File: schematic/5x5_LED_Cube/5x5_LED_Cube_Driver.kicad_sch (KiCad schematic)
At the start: 18 parts, among them J1 Conn_01x07, J2 Power, J3 Layers, Q1 DMG2305UX, Q2 DMG2305UX, Q3 DMG2305UX, Q4 DMG2305UX, Q5 DMG2305UX, U1 TLC5940NT, U2 TLC5940NT

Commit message: Added pico symbol to schematic
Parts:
- added U3: Pico, RPi_Pico:RPi_Pico_SMD_TH, symbol MCU_RaspberryPi_and_Boards:Pico
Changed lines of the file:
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@@
+    )
+  )
+  (symbol (lib_id "MCU_RaspberryPi_and_Boards:Pico") (at 78.74 148.59 0) (unit 1)
+    (in_bom yes) (on_board yes) (dnp no) (fields_autoplaced)
+    (property "Reference" "U3" (at 78.74 119.0371 0)
+      (effects (font (size 1.27 1.27)))
+    )
+    (property "Value" "Pico" (at 78.74 120.9581 0)
+      (effects (font (size 1.27 1.27)))
+    )
+    (property "Footprint" "RPi_Pico:RPi_Pico_SMD_TH" (at 78.74 148.59 90)
+      (effects (font (size 1.27 1.27)) hide)
+    )
+    (property "Datasheet" "" (at 78.74 148.59 0)
+      (effects (font (size 1.27 1.27)) hide)
+    )
+    (pin "1")
+    (pin "10")
+    (pin "11")
+    (pin "12")
+    (pin "13")
+    (pin "14")
+    (pin "15")
+    (pin "16")
+    (pin "17")
+    (pin "18")
+    (pin "19")
+    (pin "2")
+    (pin "20")
+    (pin "21")
+    (pin "22")
+    (pin "23")
+    (pin "24")
+    (pin "25")
+    (pin "26")
+    (pin "27")
+    (pin "28")
+    (pin "29")
+    (pin "3")
+    (pin "30")
+    (pin "31")
+    (pin "32")
+    (pin "33")
+    (pin "34")
+    (pin "35")
+    (pin "36")
+    (pin "37")
+    (pin "38")
+    (pin "39")
+    (pin "4")
+    (pin "40")
+    (pin "41")
+    (pin "42")
+    (pin "43")
+    (pin "5")
+    (pin "6")
+    (pin "7")
+    (pin "8")
+    (pin "9")
+    (instances
+      (project "5x5_LED_Cube_Driver"
+        (path "/3c8dc442-e2f5-4a62-b376-6357b309533c"
+          (reference "U3") (unit 1)
+        )
+      )
     )
   )

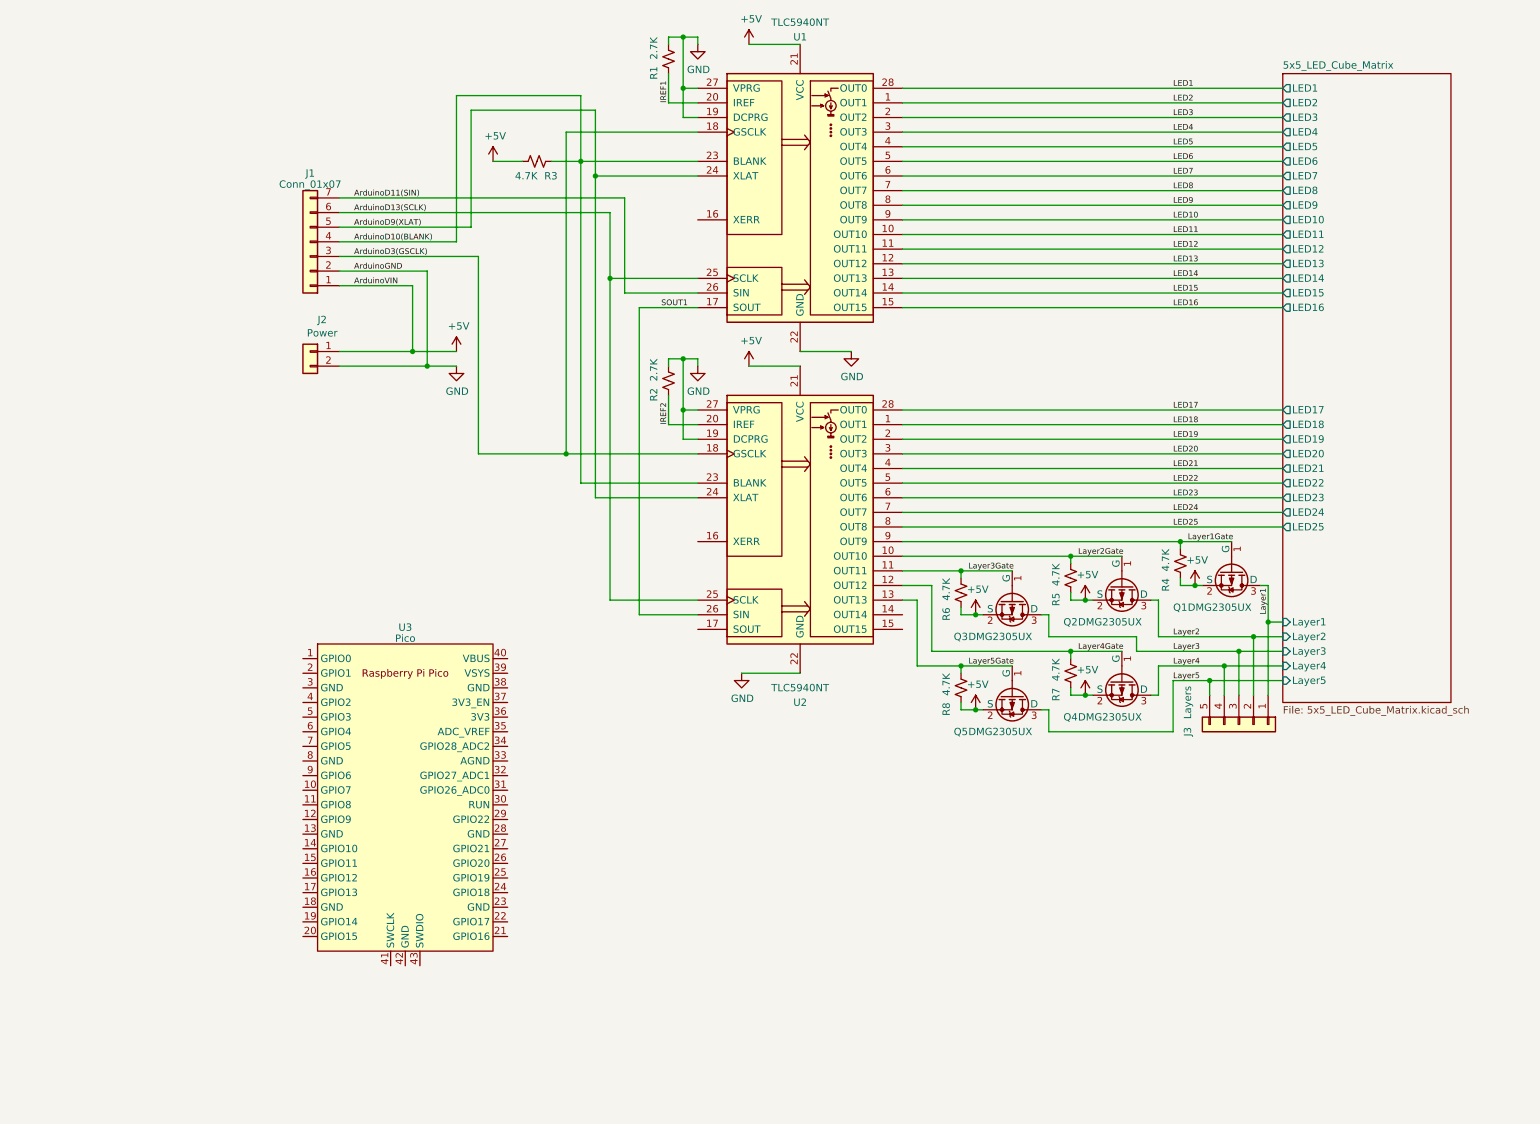
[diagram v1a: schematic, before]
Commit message: Updated schematic to include the RPi Pico and SD card module
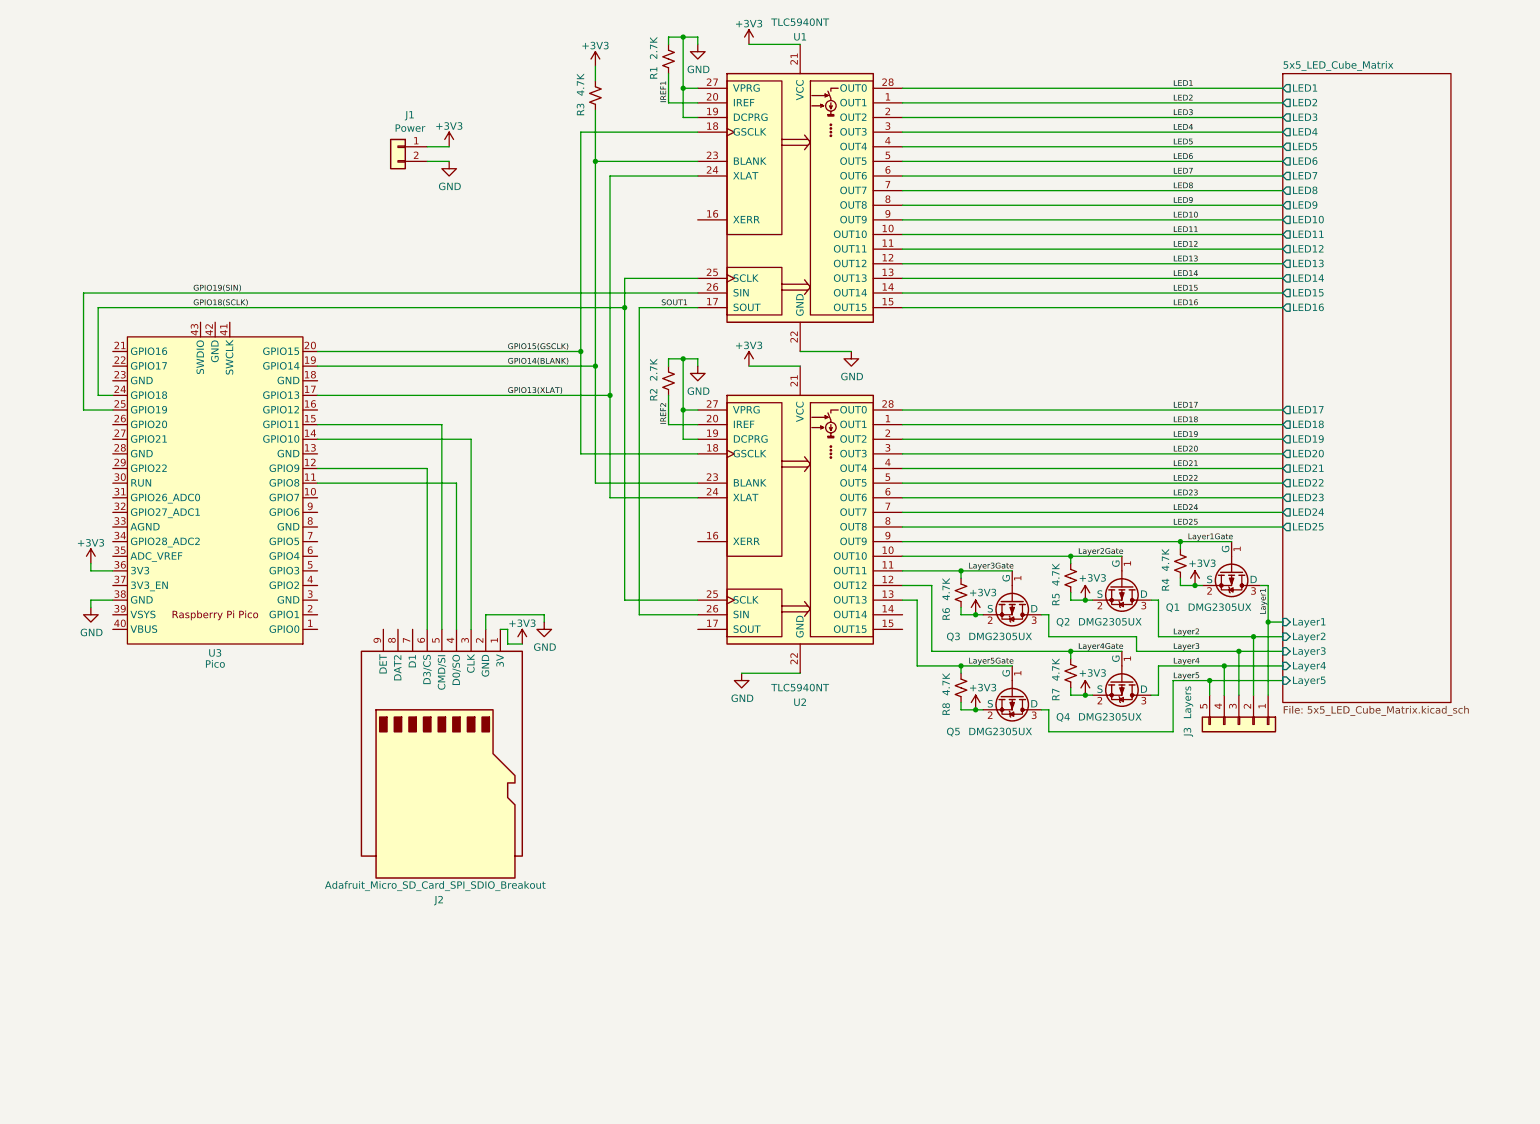
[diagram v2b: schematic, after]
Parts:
- removed J1: Conn_01x07, symbol Connector_Generic:Conn_01x07
- added J2: Adafruit_Micro_SD_Card_SPI_SDIO_Breakout, Connector_PinHeader_2.00mm:PinHeader_1x09_P2.00mm_Vertical, symbol My_Library:Adafruit_Micro_SD_Card_SPI_SDIO_Breakout
- renumbered J2 to J1
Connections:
- net +5V is gone; now on net +3V3: J1.1 (Pin_1), Q1.2 (S), Q2.2 (S), Q3.2 (S), Q4.2 (S), Q5.2 (S), R3.2, R4.1, R5.1, R6.1, R7.1, R8.1, U1.21 (VCC), U2.21 (VCC)
- net ArduinoD10(BLANK) is gone; now on net GPIO14(BLANK): R3.1, U1.23 (BLANK), U2.23 (BLANK)
- net ArduinoD11(SIN) is gone; now on net GPIO19(SIN): U1.26 (SIN)
- net ArduinoD13(SCLK) is gone; now on net GPIO18(SCLK): U1.25 (SCLK), U2.25 (SCLK)
- net ArduinoD3(GSCLK) is gone; now on net GPIO15(GSCLK): U1.18 (GSCLK), U2.18 (GSCLK)
- net ArduinoD9(XLAT) is gone; now on net GPIO13(XLAT): U1.24 (XLAT), U2.24 (XLAT)
- net GND: now also U3.38 (GND), J2.2 (GND)
- net at U3.11 (GPIO8): now also J2.4 (D0/SO)
- net at U3.12 (GPIO9): now also J2.6 (D3/CS)
- net at U3.14 (GPIO10): now also J2.3 (CLK)
- net at U3.15 (GPIO11): now also J2.5 (CMD/SI)
- net GPIO13(XLAT): now reaches U3.17 (GPIO13)
- net GPIO14(BLANK): now reaches U3.19 (GPIO14)
- net GPIO15(GSCLK): now reaches U3.20 (GPIO15)
- net GPIO18(SCLK): now reaches U3.24 (GPIO18)
- net GPIO19(SIN): now reaches U3.25 (GPIO19)
- net +3V3: now reaches U3.36 (3V3)
- net +3V3: now also J2.1 (3V)
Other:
- moved on the sheet: J1, R3, U3

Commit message: Updated schematic to wire up the SD card module to the pico
Signed-off-by: crash8229 <mu304007@gmail.com>
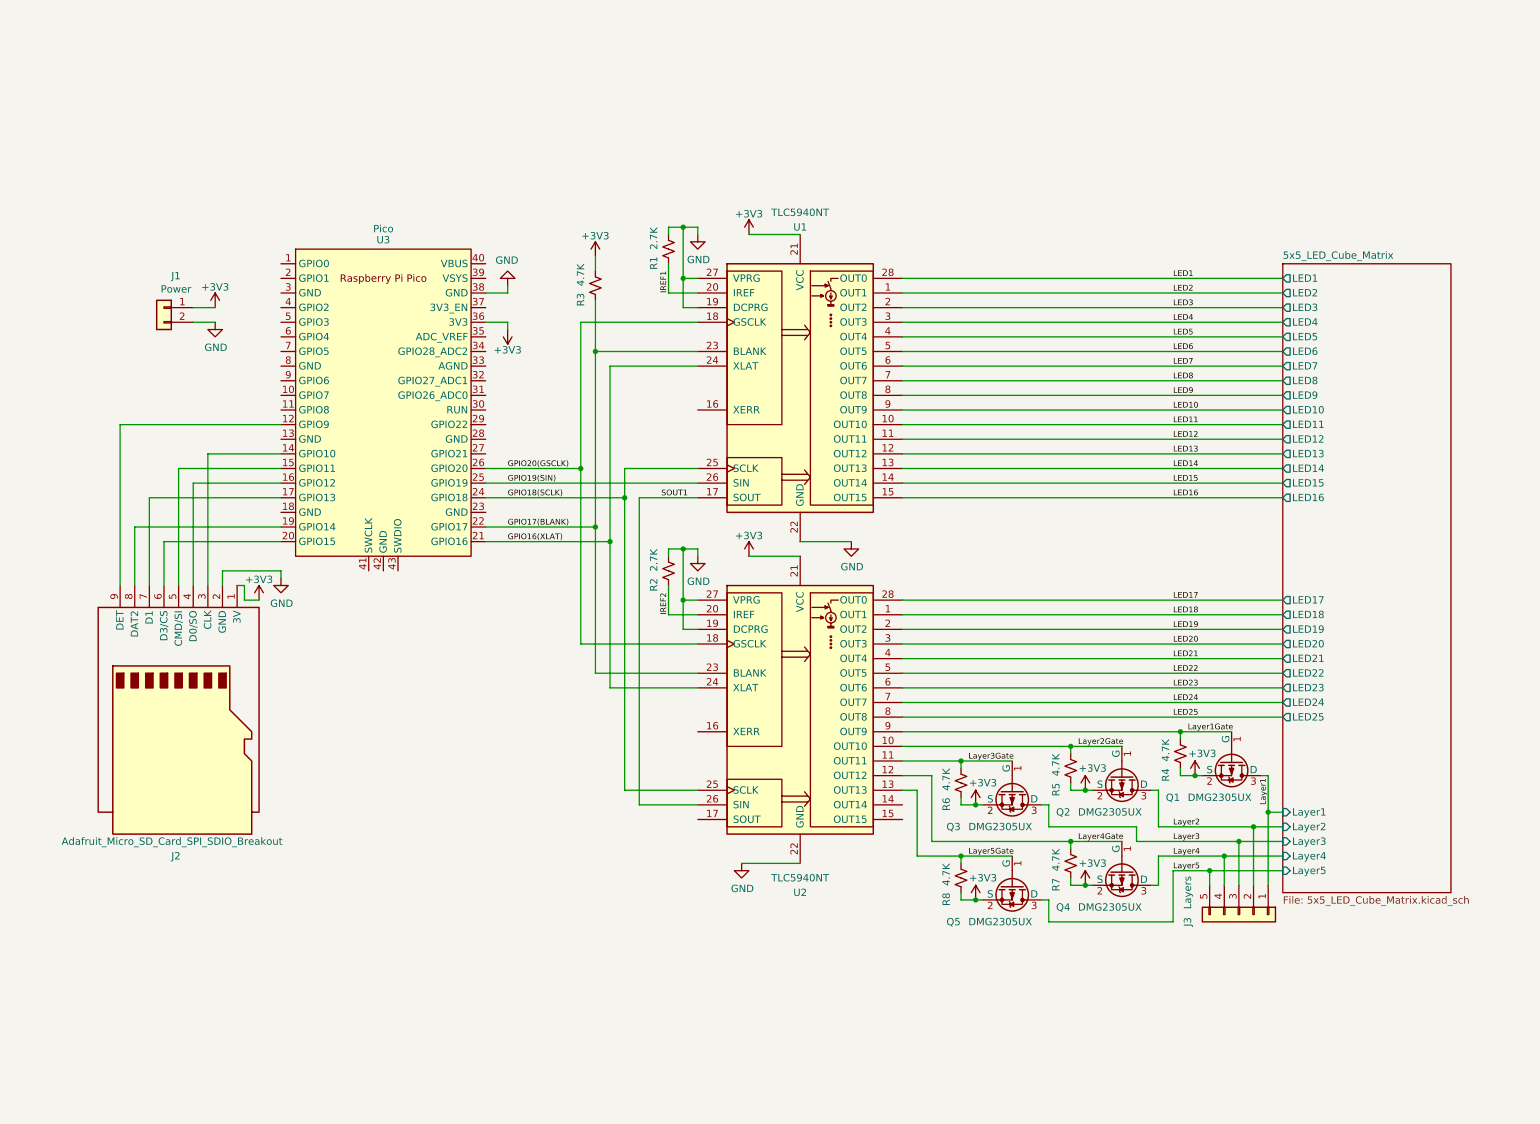
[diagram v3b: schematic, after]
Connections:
- net at J2.4 (D0/SO): now also U3.16 (GPIO12); no longer U3.11 (GPIO8)
- net at J2.6 (D3/CS): now also U3.20 (GPIO15); no longer U3.12 (GPIO9)
- net at J2.7 (D1): now also U3.17 (GPIO13)
- net at J2.8 (DAT2): now also U3.19 (GPIO14)
- net at J2.9 (DET): now also U3.12 (GPIO9)
- net GPIO16(XLAT): now reaches U3.21 (GPIO16)
- net GPIO16(XLAT): now also U1.24 (XLAT), U2.24 (XLAT)
- net GPIO17(BLANK): now reaches U3.22 (GPIO17)
- net GPIO17(BLANK): now also R3.1, U1.23 (BLANK), U2.23 (BLANK)
- net GPIO20(GSCLK): now reaches U3.26 (GPIO20)
- net GPIO20(GSCLK): now also U1.18 (GSCLK), U2.18 (GSCLK)
- removed net GPIO13(XLAT): U1.24 (XLAT), U2.24 (XLAT), U3.17 (GPIO13)
- removed net GPIO14(BLANK): R3.1, U1.23 (BLANK), U2.23 (BLANK), U3.19 (GPIO14)
- removed net GPIO15(GSCLK): U1.18 (GSCLK), U2.18 (GSCLK), U3.20 (GPIO15)
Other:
- moved on the sheet: J1, J2, J3, Q1, Q2, Q3, Q4, Q5, R1, R2, R3, R4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

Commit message: Updated schematic and footprints
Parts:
- added C1, C2, C3, C4: 0.1µF, Capacitor_SMD:C_0402_1005Metric_Pad0.74x0.62mm_HandSolder, symbol Device:C_Small
- J1: footprint Connector_PinHeader_2.00mm:PinHeader_1x02_P2.00mm_Vertical -> Connector_PinSocket_2.54mm:PinSocket_1x02_P2.54mm_Vertical
- J2: footprint Connector_PinHeader_2.00mm:PinHeader_1x09_P2.00mm_Vertical -> My_Library:Adafruit_Micro_SD_Card_SPI_SDIO_Breakout
- J3: footprint Connector_PinHeader_2.00mm:PinHeader_1x05_P2.00mm_Vertical -> Connector_PinSocket_2.54mm:PinSocket_1x05_P2.54mm_Vertical
- U3: footprint RPi_Pico:RPi_Pico_SMD_TH -> MCU_RaspberryPi_and_Boards:RPi_Pico_SMD_TH
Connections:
- net +3V3: now also U3.39 (VSYS), C1.1, C2.2, C3.1, C4.2; no longer U3.36 (3V3)
- net GND: now also C1.2, C2.1, C3.2, C4.1
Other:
- moved on the sheet: J1, J2, R1, R3, U1, U3
